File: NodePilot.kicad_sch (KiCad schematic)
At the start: 39 parts, among them K1 SRD-05VDC-SL-C, Q1 2N3904, Q2 2N2222, Q4 2N3904, T1 1:1 600R, T2 1:1 600R, U1 PC817, U2 PC817, U3 B0505S-1WR2

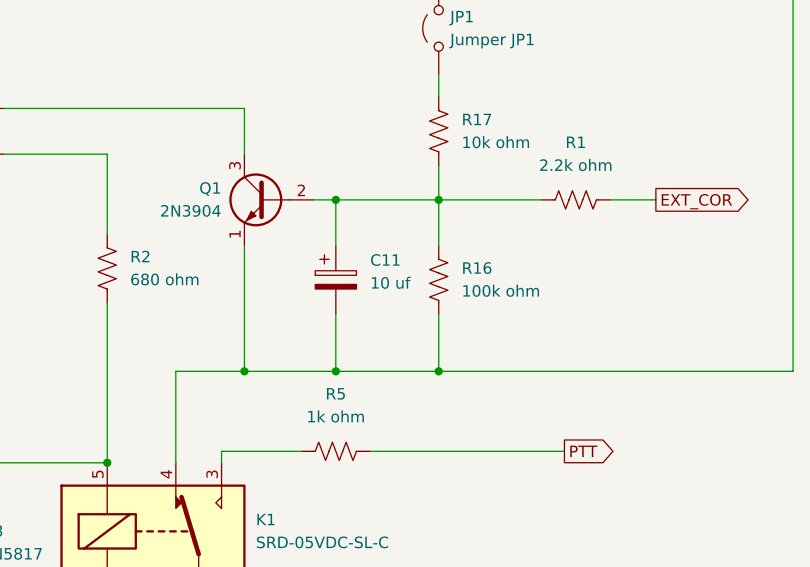
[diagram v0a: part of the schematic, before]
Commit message: reduce filter capacitor
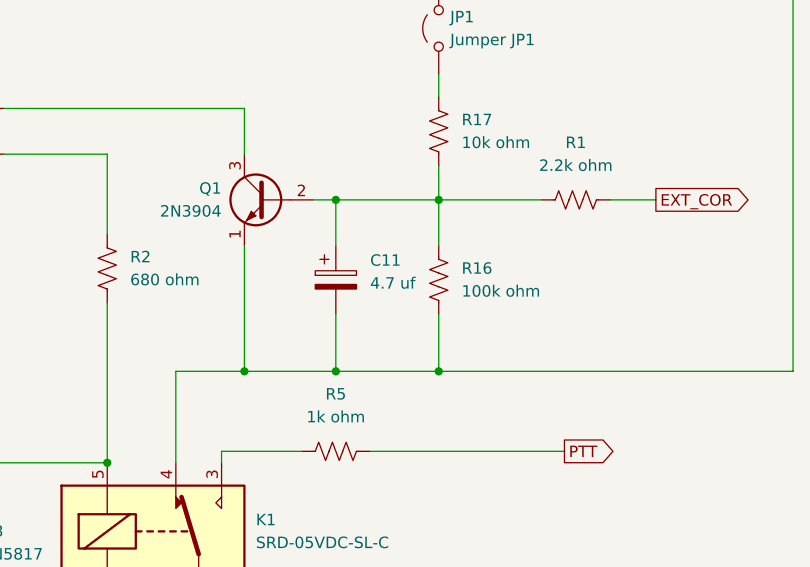
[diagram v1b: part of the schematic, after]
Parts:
- C11: value 10 uf -> 4.7 uf
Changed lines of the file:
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@@
 			)
 		)
-		(property "Value" "10 uf"
+		(property "Value" "4.7 uf"
 			(at 187.96 109.6009 0)
 			(show_name no)

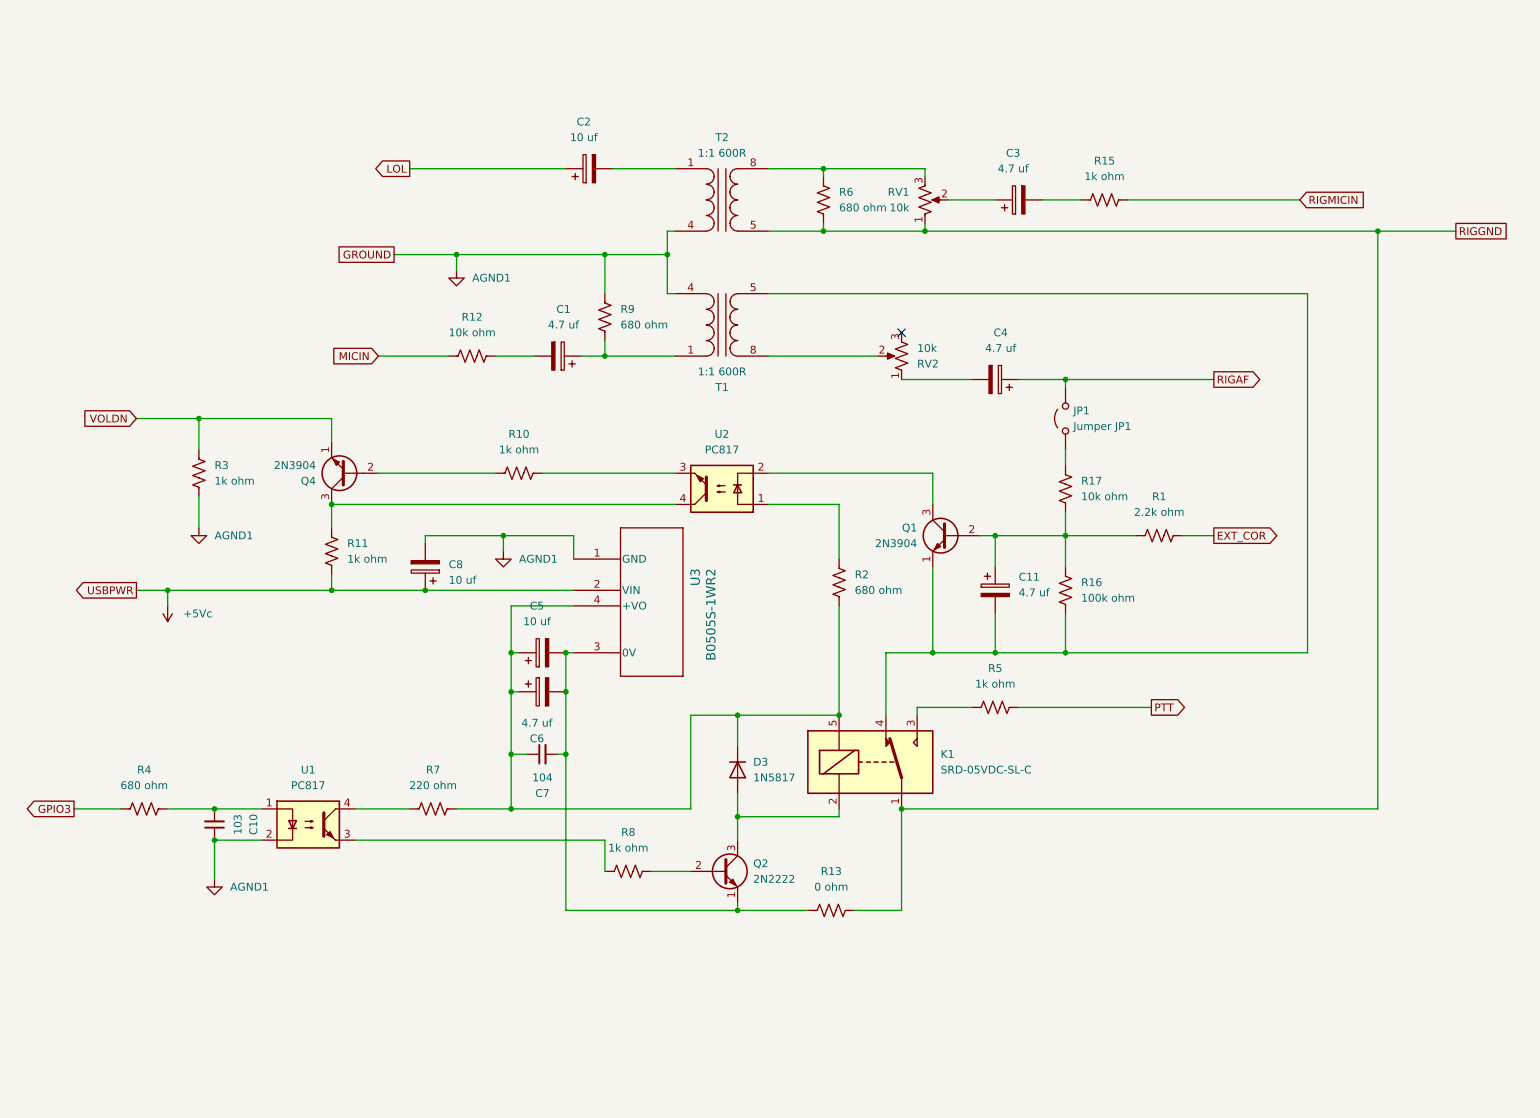
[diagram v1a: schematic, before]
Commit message: for audio stability
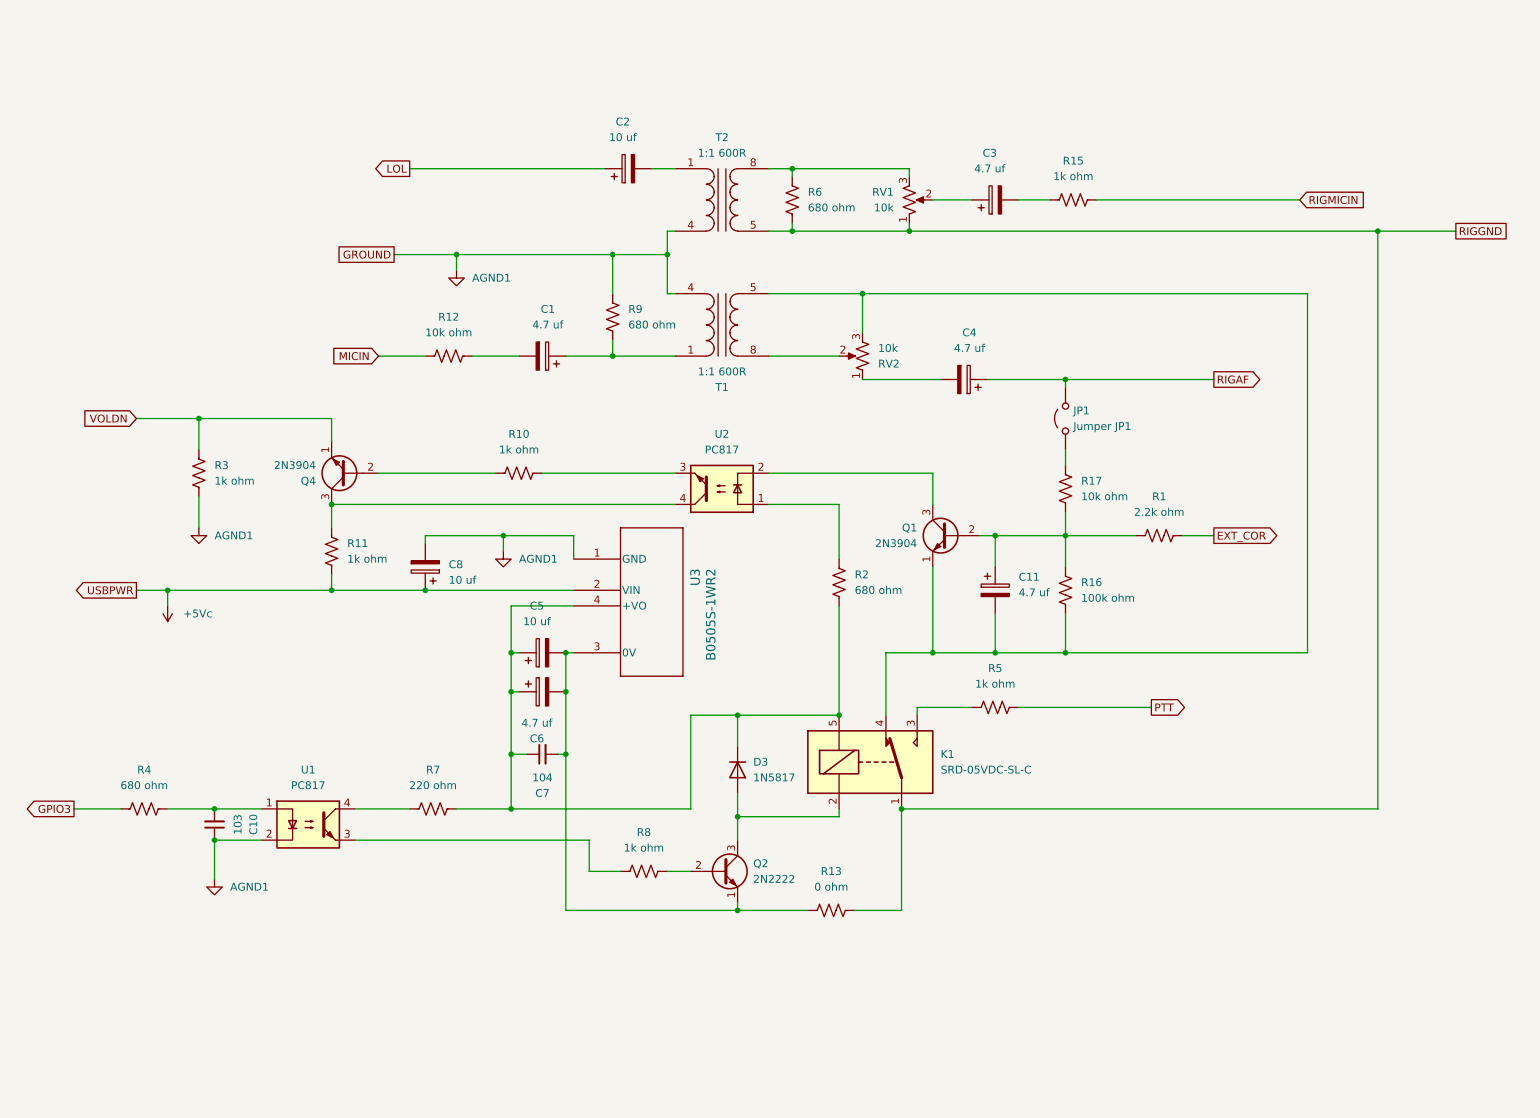
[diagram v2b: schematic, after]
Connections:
- net at C11.2, K1.4, Q1.1 (E)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: now also RV2.3
- no-connect marks 1 -> 0
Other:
- moved on the sheet: C1, C2, C3, C4, R12, R15, R6, R8, R9, RV1

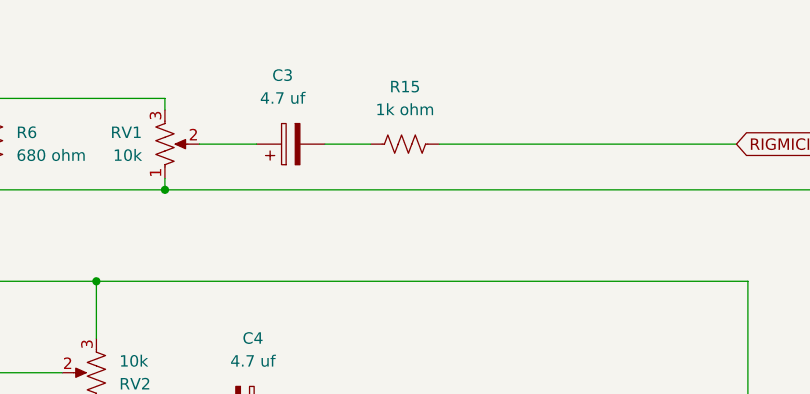
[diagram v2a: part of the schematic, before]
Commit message: protection resistor value reduce
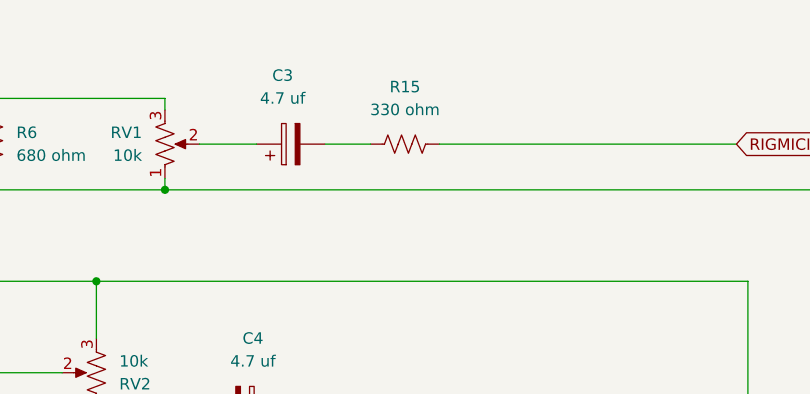
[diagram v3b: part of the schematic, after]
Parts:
- R15: value 1k ohm -> 330 ohm
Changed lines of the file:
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@@
 			)
 		)
-		(property "Value" "1k ohm"
+		(property "Value" "330 ohm"
 			(at 196.85 41.91 90)
 			(show_name no)

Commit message: protection resistor value
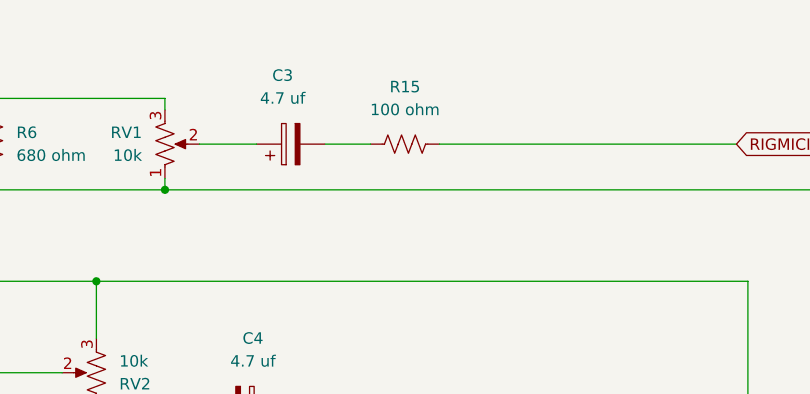
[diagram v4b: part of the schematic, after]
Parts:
- R15: value 330 ohm -> 100 ohm
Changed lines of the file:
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@@
 			)
 		)
-		(property "Value" "330 ohm"
+		(property "Value" "100 ohm"
 			(at 196.85 41.91 90)
 			(show_name no)

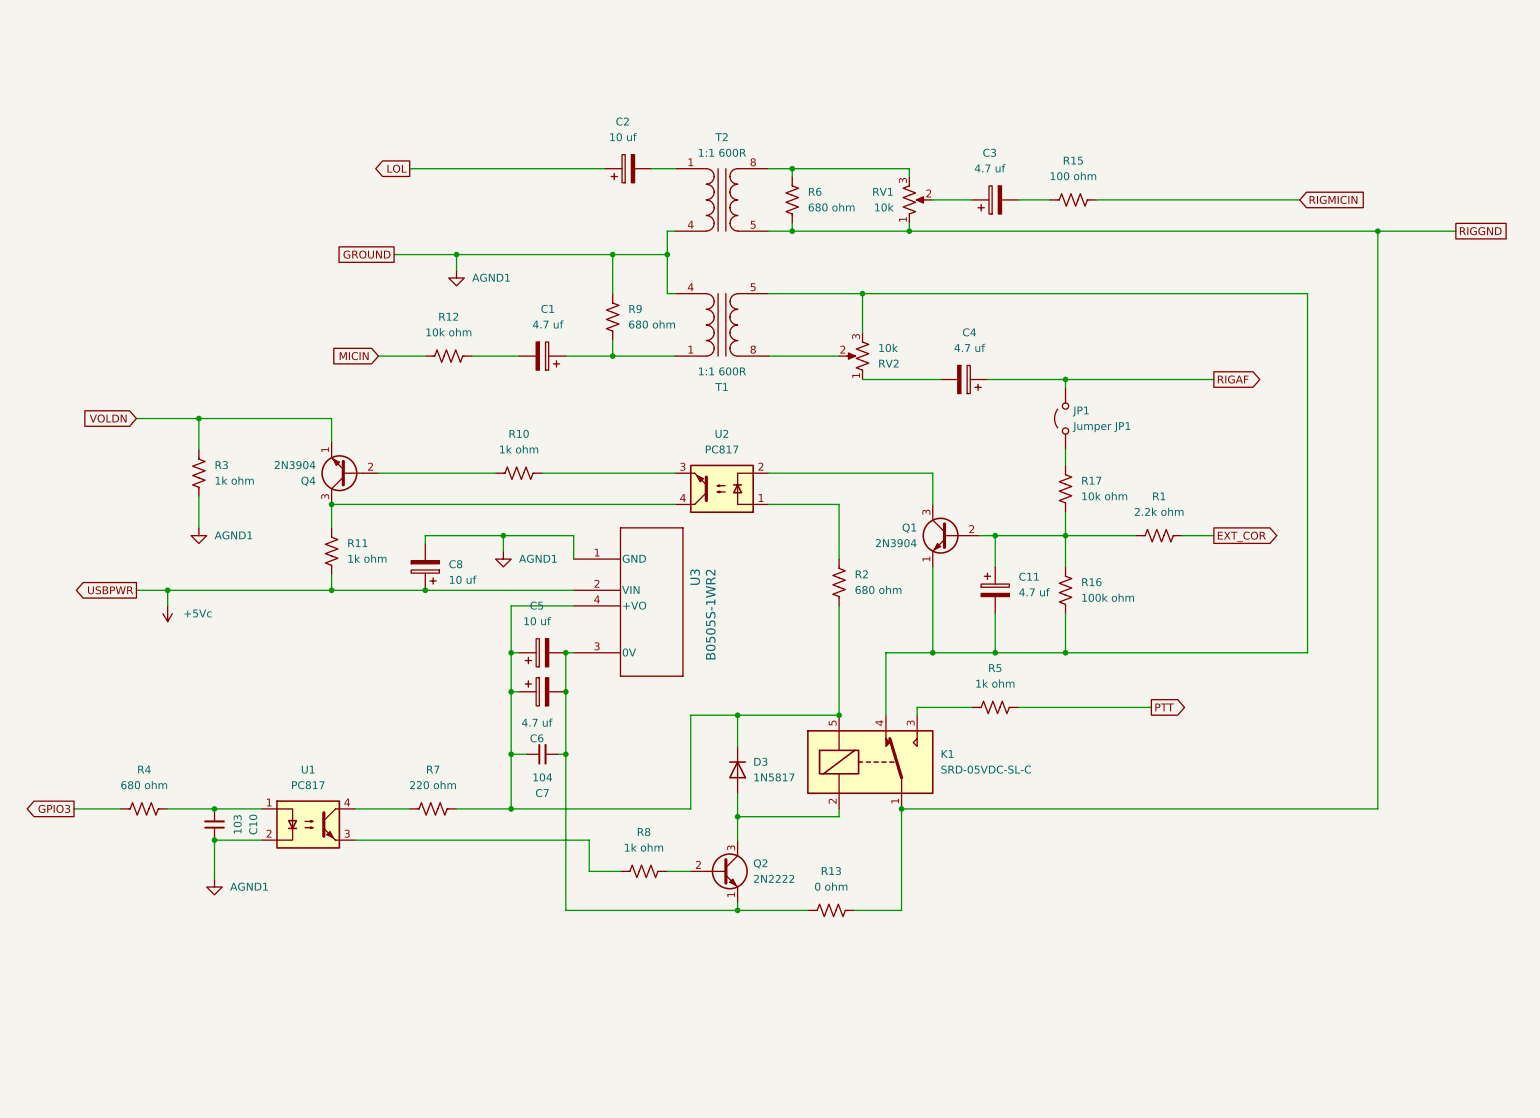
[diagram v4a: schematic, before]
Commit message: NodePilot Advance prerelease (#7)
* node pilot advanced

* reducing noise while only PTT is pressed.

* correct v level

---------

Co-authored-by: Tushar <skydel.net@gmail.com>
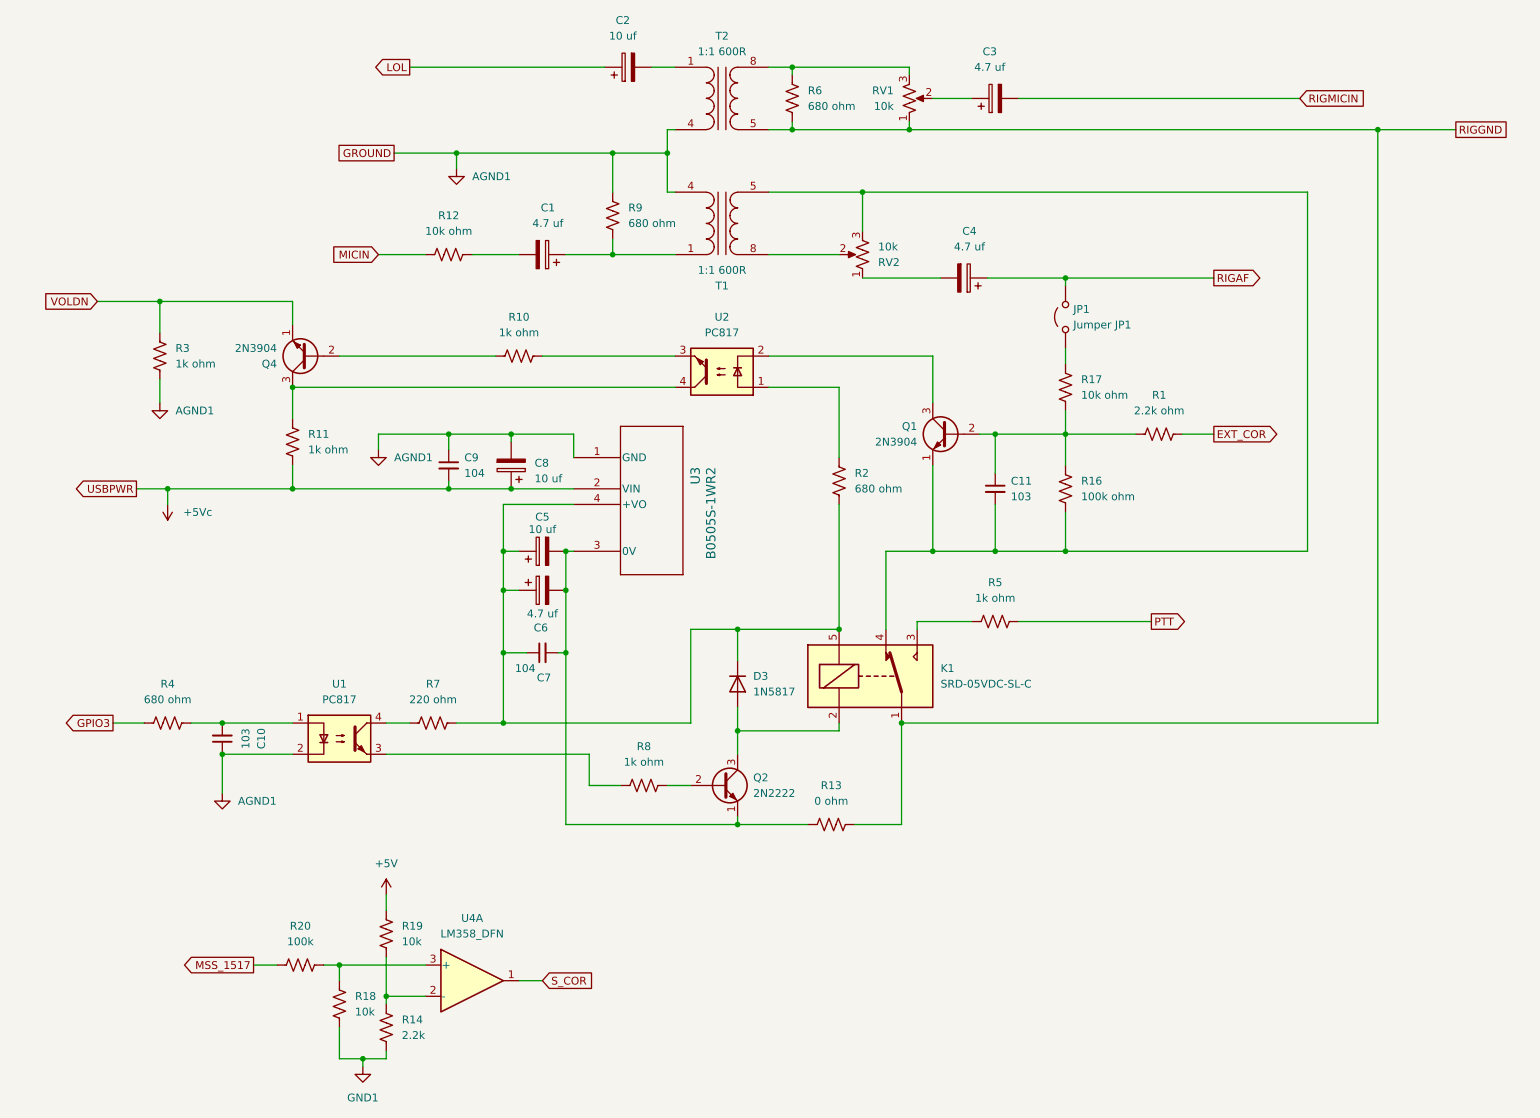
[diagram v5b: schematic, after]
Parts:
- removed C11: 4.7 uf, symbol Device:C_Polarized
- removed R15: 100 ohm, symbol Device:R_US
- added C11: 103, symbol Device:C_Small
- added C9: 104, symbol Device:C_Small
- added R14: 2.2k, symbol Device:R_US
- added R18, R19: 10k, symbol Device:R_US
- added R20: 100k, symbol Device:R_US
- added U4: LM358_DFN, Package_DFN_QFN:DFN-8-1EP_2x2mm_P0.5mm_EP1.05x1.75mm, symbol Amplifier_Operational:LM358_DFN
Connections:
- net +5Vc: now also C9.2
- net AGND1: now also C9.1
- net RIGMICIN: now also C3.2
- net at K1.4, Q1.1 (E), R16.2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: now also C11.2
- net at Q1.2 (B), R1.1, R16.1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: now also C11.1
- new net: R14.1, R19.2, U4.2 (-)
- new net: R18.1, R20.2, U4.3 (+)
- new net +5V: R19.1
- new net GND1: R14.2, R18.2
- new net MSS_1517: R20.1
- new net S_COR: U4.1
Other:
- moved on the sheet: C1, C10, C2, C3, C4, C5, C6, C7, C8, D3, JP1, K1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

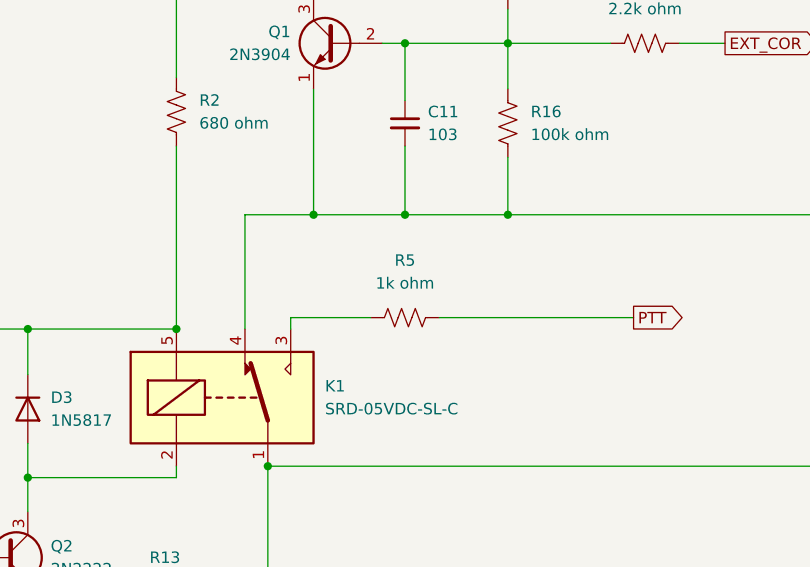
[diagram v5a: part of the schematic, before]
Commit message: reduce ptt protection resistor to 2.2 ohm
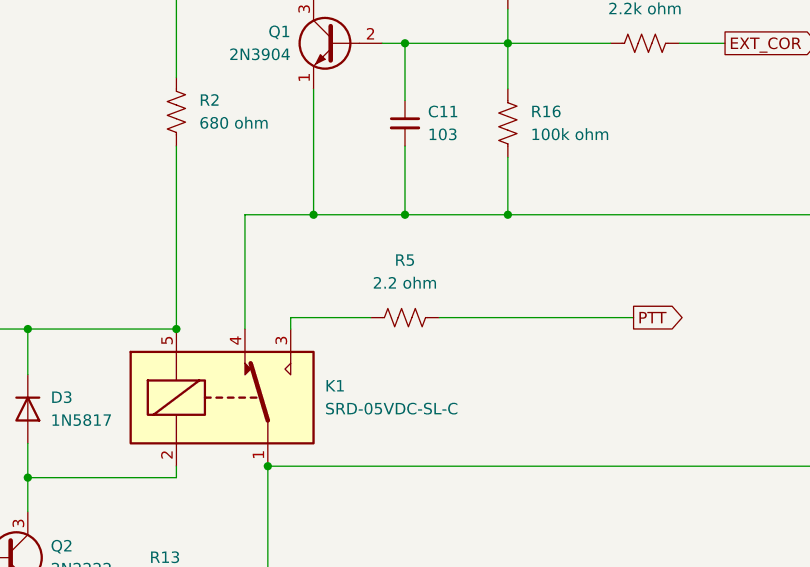
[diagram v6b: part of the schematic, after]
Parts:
- R5: value 1k ohm -> 2.2 ohm
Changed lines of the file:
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@@
 			)
 		)
-		(property "Value" "1k ohm"
+		(property "Value" "2.2 ohm"
 			(at 184.15 110.49 90)
 			(show_name no)
